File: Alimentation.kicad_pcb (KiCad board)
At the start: 2 copper layers, 50 x 50 mm, 21 parts, among them P1 Prise_Equilibrage, P2 Prise_Alim, P3 Prise_Batterie, P4 ConnecteurBippeur, P5 CONN_01X04, P6 CONN_01X02, P7 CONN_01X02, P8 CONN_01X02, U1 LD1084V

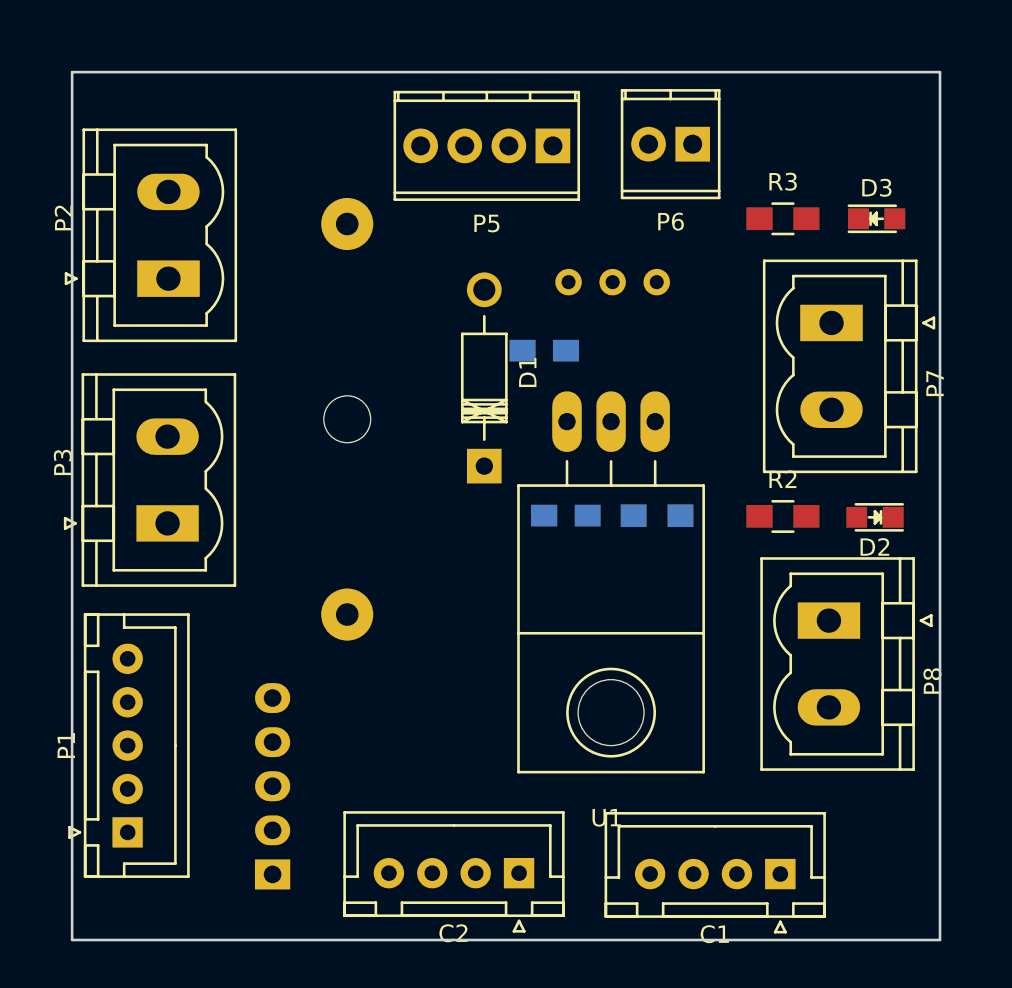
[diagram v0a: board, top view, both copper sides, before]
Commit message: prise en compte des changements dans la lib perso
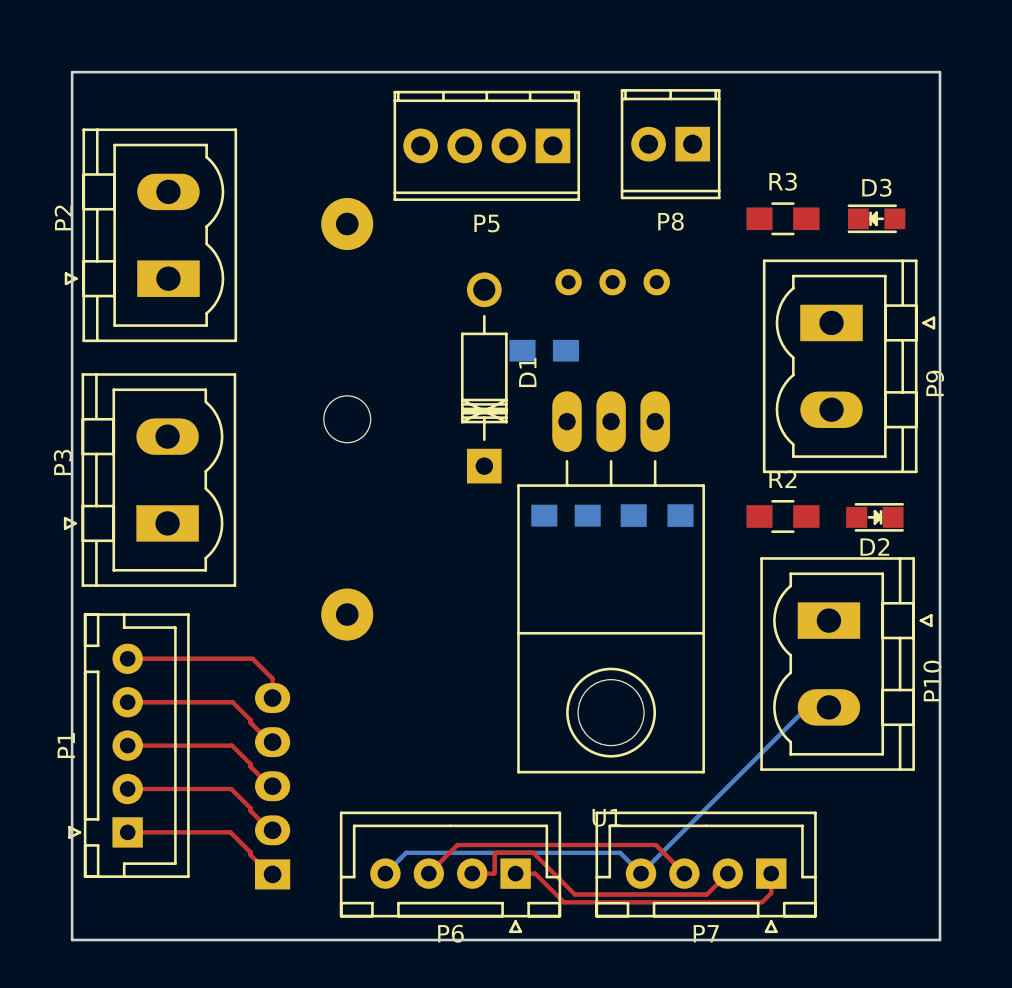
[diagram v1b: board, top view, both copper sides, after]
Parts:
- removed the C1 at (140.8, 96.2)
- removed the C2 at (125.8, 96.2)
- added P6: CAN_conn, Connectors_JST:JST_XH_B04B-XH-A_04x2.50mm_Straight, F.Cu at (125.5, 96.2)
- added P7: CAN_conn, Connectors_JST:JST_XH_B04B-XH-A_04x2.50mm_Straight, F.Cu at (140.3, 96.2)
- renumbered C3 to C1, C4 to C2, P8 to P10, P6 to P8, P7 to P9
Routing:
- net GND: track 0.00 -> 30.5 mm
- net CAN_H: track 0.00 -> 17.3 mm
- net +9V: track 0.00 -> 16.8 mm
- net CAN_L: track 0.00 -> 16.1 mm
- net Net-(P1-Pad5): track 0.00 -> 9.94 mm
- net Net-(P1-Pad1): track 0.00 -> 9.44 mm
- net Net-(P1-Pad2): track 0.00 -> 9.43 mm
- net Net-(P1-Pad3): track 0.00 -> 9.41 mm
- net Net-(P1-Pad4): track 0.00 -> 9.39 mm

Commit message: routage préliminaire (dirty)
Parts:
- moved C1 2.83 mm to (130.0, 66.0), turned to 0 degrees
- turned D3 to 180 degrees
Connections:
- P5 pad 1: Net-(F1-Pad2) -> GND
- P5 pad 2: GND -> Net-(F1-Pad2)
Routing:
- net GND: track 30.5 -> 160.3 mm
- net +9V: track 16.8 -> 66.7 mm
- net Net-(P3-Pad2): track 0.00 -> 27.2 mm
- net Net-(C1-Pad1): track 0.00 -> 23.7 mm
- net Net-(P2-Pad2): track 0.00 -> 16.4 mm
- net Non_régulé: track 0.00 -> 15.4 mm
- net Net-(R1-Pad2): track 0.00 -> 14.7 mm
- net Net-(D1-Pad1): track 0.00 -> 11.8 mm
- net Net-(F1-Pad2): track 0.00 -> 11.2 mm
- net Net-(D3-Pad2): track 0.00 -> 3.00 mm
- net Net-(D2-Pad2): track 0.00 -> 2.92 mm

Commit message: met la masse à l'extérieur
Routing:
- net GND: track 160.3 -> 171.0 mm
- net +9V: track 66.7 -> 69.5 mm
- net CAN_L: track 16.1 -> 16.9 mm
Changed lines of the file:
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@@
   (general
     (links 38)
-    (no_connects 15)
-    (area 99.924999 49.924999 150.075001 100.075001)
+    (no_connects 0)
+    (area 67.150001 22.3 150.825 102.395)
     (thickness 1.6)
     (drawings 6)
-    (tracks 133)
+    (tracks 130)
     (zones 0)
     (modules 21)
@@
     (arrow2b (pts (xy 75 50) (xy 75.586421 51.126504)))
   )
+  (segment (start 127.225 92.575) (end 125.55 94.25) (width 0.25) (layer F.Cu) (net 1))
+  (segment (start 125.55 94.25) (end 125.55 96.175) (width 0.25) (layer F.Cu) (net 1))
+  (segment (start 137.8 92.575) (end 127.225 92.575) (width 0.25) (layer F.Cu) (net 1))
+  (segment (start 140.275 96.175) (end 140.275 95.05) (width 0.25) (layer F.Cu) (net 1))
+  (segment (start 140.275 95.05) (end 137.8 92.575) (width 0.25) (layer F.Cu) (net 1))
   (segment (start 129.7 75.55) (end 130.7 75.55) (width 0.25) (layer B.Cu) (net 1))
   (segment (start 130.7 75.55) (end 131.05 75.2) (width 0.25) (layer B.Cu) (net 1))
@@
   (segment (start 139.6 75.6) (end 139.6 78.35) (width 0.25) (layer F.Cu) (net 1))
   (segment (start 139.6 78.35) (end 142.85 81.6) (width 0.25) (layer F.Cu) (net 1))
-  (segment (start 126.675 96.175) (end 125.55 96.175) (width 0.25) (layer F.Cu) (net 1))
-  (segment (start 139.749988 97.825012) (end 128.325012 97.825012) (width 0.25) (layer F.Cu) (net 1))
-  (segment (start 140.275 97.3) (end 139.749988 97.825012) (width 0.25) (layer F.Cu) (net 1))
-  (segment (start 140.275 96.175) (end 140.275 97.3) (width 0.25) (layer F.Cu) (net 1))
-  (segment (start 128.325012 97.825012) (end 126.675 96.175) (width 0.25) (layer F.Cu) (net 1))
-  (segment (start 135.275 96.175) (end 133.624988 94.524988) (width 0.25) (layer F.Cu) (net 2))
-  (segment (start 133.624988 94.524988) (end 122.200012 94.524988) (width 0.25) (layer F.Cu) (net 2))
-  (segment (start 122.200012 94.524988) (end 121.424999 95.300001) (width 0.25) (layer F.Cu) (net 2))
-  (segment (start 121.424999 95.300001) (end 120.55 96.175) (width 0.25) (layer F.Cu) (net 2))
-  (segment (start 124.349999 96.112437) (end 124.287436 96.175) (width 0.25) (layer F.Cu) (net 3))
-  (segment (start 124.349999 95.039999) (end 124.349999 96.112437) (width 0.25) (layer F.Cu) (net 3))
-  (segment (start 126.563595 94.974999) (end 124.414999 94.974999) (width 0.25) (layer F.Cu) (net 3))
-  (segment (start 128.963597 97.375001) (end 126.563595 94.974999) (width 0.25) (layer F.Cu) (net 3))
-  (segment (start 136.574999 97.375001) (end 128.963597 97.375001) (width 0.25) (layer F.Cu) (net 3))
-  (segment (start 137.775 96.175) (end 136.574999 97.375001) (width 0.25) (layer F.Cu) (net 3))
-  (segment (start 124.287436 96.175) (end 123.05 96.175) (width 0.25) (layer F.Cu) (net 3))
-  (segment (start 124.414999 94.974999) (end 124.349999 95.039999) (width 0.25) (layer F.Cu) (net 3))
+  (segment (start 121.112564 97.975) (end 133.475 97.975) (width 0.25) (layer B.Cu) (net 2))
+  (segment (start 133.475 97.975) (end 135.275 96.175) (width 0.25) (layer B.Cu) (net 2))
+  (segment (start 120.55 96.175) (end 120.55 97.412436) (width 0.25) (layer B.Cu) (net 2))
+  (segment (start 120.55 97.412436) (end 121.112564 97.975) (width 0.25) (layer B.Cu) (net 2))
+  (segment (start 123.05 96.175) (end 125.65 93.575) (width 0.25) (layer B.Cu) (net 3))
+  (segment (start 125.65 93.575) (end 135.175 93.575) (width 0.25) (layer B.Cu) (net 3))
+  (segment (start 135.175 93.575) (end 137.775 96.175) (width 0.25) (layer B.Cu) (net 3))
+  (segment (start 130.4 98.55) (end 120.425 98.55) (width 0.25) (layer F.Cu) (net 4))
+  (segment (start 120.425 98.55) (end 118.05 96.175) (width 0.25) (layer F.Cu) (net 4))
+  (segment (start 132.775 96.175) (end 130.4 98.55) (width 0.25) (layer F.Cu) (net 4))
+  (segment (start 142.65 98.55) (end 135.15 98.55) (width 0.25) (layer F.Cu) (net 4))
+  (segment (start 135.15 98.55) (end 132.775 96.175) (width 0.25) (layer F.Cu) (net 4))
+  (segment (start 143.6 97.6) (end 142.65 98.55) (width 0.25) (layer F.Cu) (net 4))
+  (segment (start 143.6 86.6) (end 143.6 97.6) (width 0.25) (layer F.Cu) (net 4))
   (segment (start 139.9 64.25) (end 139.9 67.3) (width 0.25) (layer B.Cu) (net 4))
   (segment (start 137.575 76.125) (end 137.575 74.875) (width 0.25) (layer B.Cu) (net 4))
@@
   (segment (start 147.29804 75.65) (end 147.29804 72.24804) (width 0.25) (layer F.Cu) (net 4))
   (segment (start 147.29804 72.24804) (end 144.5 69.45) (width 0.25) (layer F.Cu) (net 4))
-  (segment (start 132.775 96.175) (end 142.35 86.6) (width 0.25) (layer B.Cu) (net 4))
   (segment (start 142.35 86.6) (end 143.6 86.6) (width 0.25) (layer B.Cu) (net 4))
-  (segment (start 132.775 96.175) (end 131.574999 94.974999) (width 0.25) (layer B.Cu) (net 4))
-  (segment (start 119.250001 94.974999) (end 118.924999 95.300001) (width 0.25) (layer B.Cu) (net 4))
-  (segment (start 131.574999 94.974999) (end 119.250001 94.974999) (width 0.25) (layer B.Cu) (net 4))
-  (segment (start 118.924999 95.300001) (end 118.05 96.175) (width 0.25) (layer B.Cu) (net 4))
   (segment (start 115.85 81.25) (end 123.74746 73.35254) (width 0.25) (layer F.Cu) (net 5))
   (segment (start 123.74746 73.35254) (end 123.74746 72.7) (width 0.25) (layer F.Cu) (net 5))

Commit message: routage terminé ?
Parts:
- F1, R1, RV1: moved to F.Cu
- P10, P2, P3, P9: footprint Connectors_Phoenix:PhoenixContact_MSTBVA-G_02x5.00mm_Vertical -> Connectors_Phoenix:PhoenixContact_MC-G_02x3.50mm_Angled
- P5: footprint Terminal_Blocks:TerminalBlock_Pheonix_MPT-2.54mm_4pol -> Connectors_Phoenix:PhoenixContact_MC-G_04x3.50mm_Angled
- P8: footprint Terminal_Blocks:TerminalBlock_Pheonix_MPT-2.54mm_2pol -> Connectors_Phoenix:PhoenixContact_MC-G_02x3.50mm_Angled
- moved D1 15.3 mm to (123.0, 88.0)
- moved R3 11.1 mm to (140.0, 69.5), turned to 90 degrees
- moved P8 10.4 mm to (146.0, 56.0)
- moved C2 9.18 mm to (130.0, 66.5)
- moved P9 7.55 mm to (144.0, 72.0), turned to 90 degrees
- moved P5 7.51 mm to (135.0, 56.0)
- moved R1 6.03 mm to (137.0, 70.5), turned to 90 degrees
- moved P3 6.02 mm to (106.0, 70.0), turned to 270 degrees
- moved D3 5.87 mm to (144.5, 64.0)
- moved C1 5.44 mm to (125.5, 69.0), turned to 90 degrees
- moved P10 4.92 mm to (144.0, 86.5), turned to 90 degrees
- moved P2 3.93 mm to (106.0, 58.0), turned to 270 degrees
- moved D2 3.47 mm to (144.5, 78.7)
- moved P1 3.05 mm to (105.2, 91.5)
- moved R2 2.02 mm to (139.5, 77.0)
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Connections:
- P10 pad 1: +9V -> GND
- P10 pad 2: GND -> +9V
- P9 pad 1: Non_régulé -> GND
- P9 pad 2: GND -> Non_régulé
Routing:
- net Net-(C1-Pad1): track 23.7 -> 41.1 mm
- net Net-(F1-Pad2): track 11.2 -> 19.4 mm
- net Net-(P2-Pad2): track 16.4 -> 21.3 mm
- net CAN_H: track 16.9 -> 21.7 mm
- net CAN_L: track 16.9 -> 21.6 mm
- net Net-(P3-Pad2): track 27.2 -> 31.3 mm
- net GND: track 171.0 -> 174.4 mm
- net Non_régulé: track 15.4 -> 18.3 mm
- net Net-(D3-Pad2): track 3.00 -> 5.76 mm
- net +9V: track 69.5 -> 71.7 mm
- net Net-(R1-Pad2): track 14.7 -> 12.6 mm
- net Net-(P1-Pad5): track 9.94 -> 8.03 mm
- net Net-(P1-Pad2): track 9.43 -> 8.08 mm
- net Net-(P1-Pad4): track 9.39 -> 8.04 mm
- net Net-(P1-Pad3): track 9.41 -> 8.06 mm
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- added copper zone on B.Cu, net GND
- added copper zone on F.Cu, net GND
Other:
- net class DRC added: clearance 0.65, trace_width 0.5, via_dia 0.6, via_drill 0.4
- net class Interm added: clearance 0.4, trace_width 0.5, via_dia 0.6, via_drill 0.4
- net class PWR added: clearance 0.8, trace_width 1.5, via_dia 0.6, via_drill 0.4

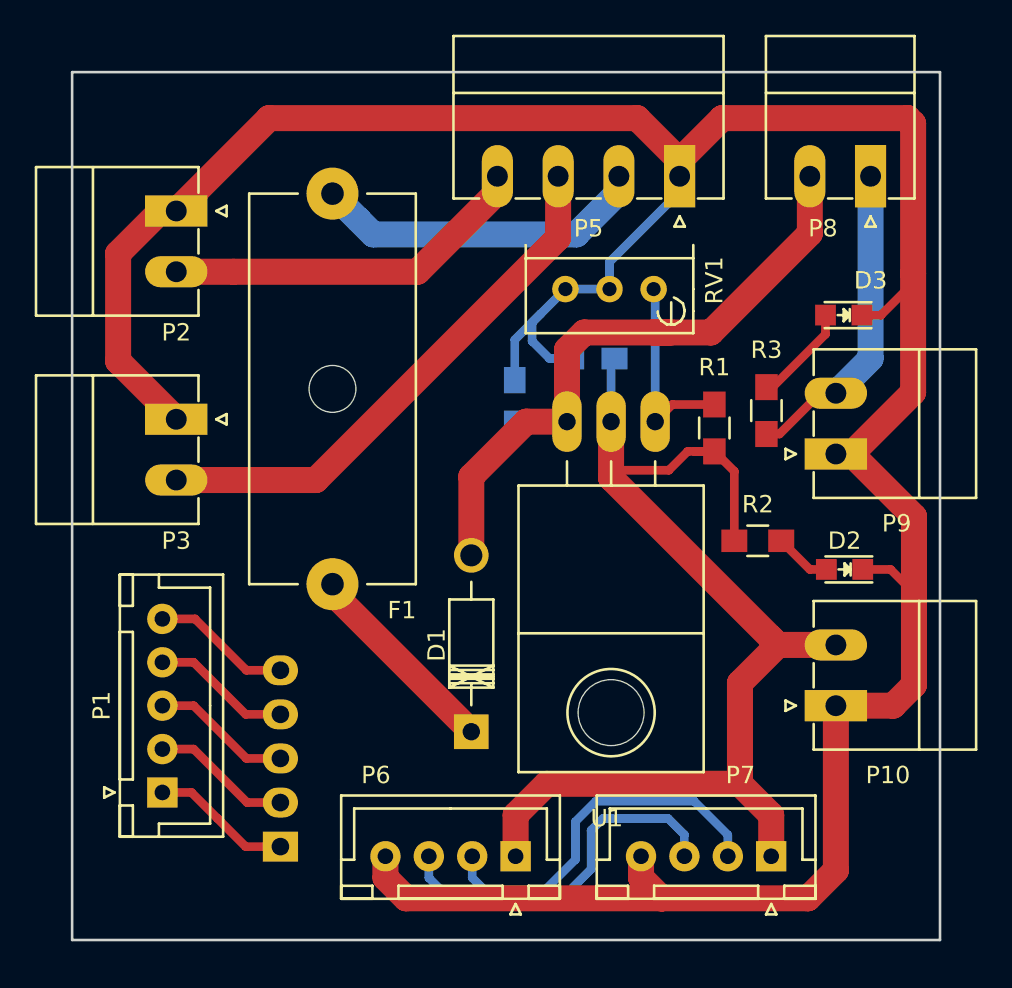
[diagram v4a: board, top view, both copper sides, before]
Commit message: ajoute les trous pour les vis
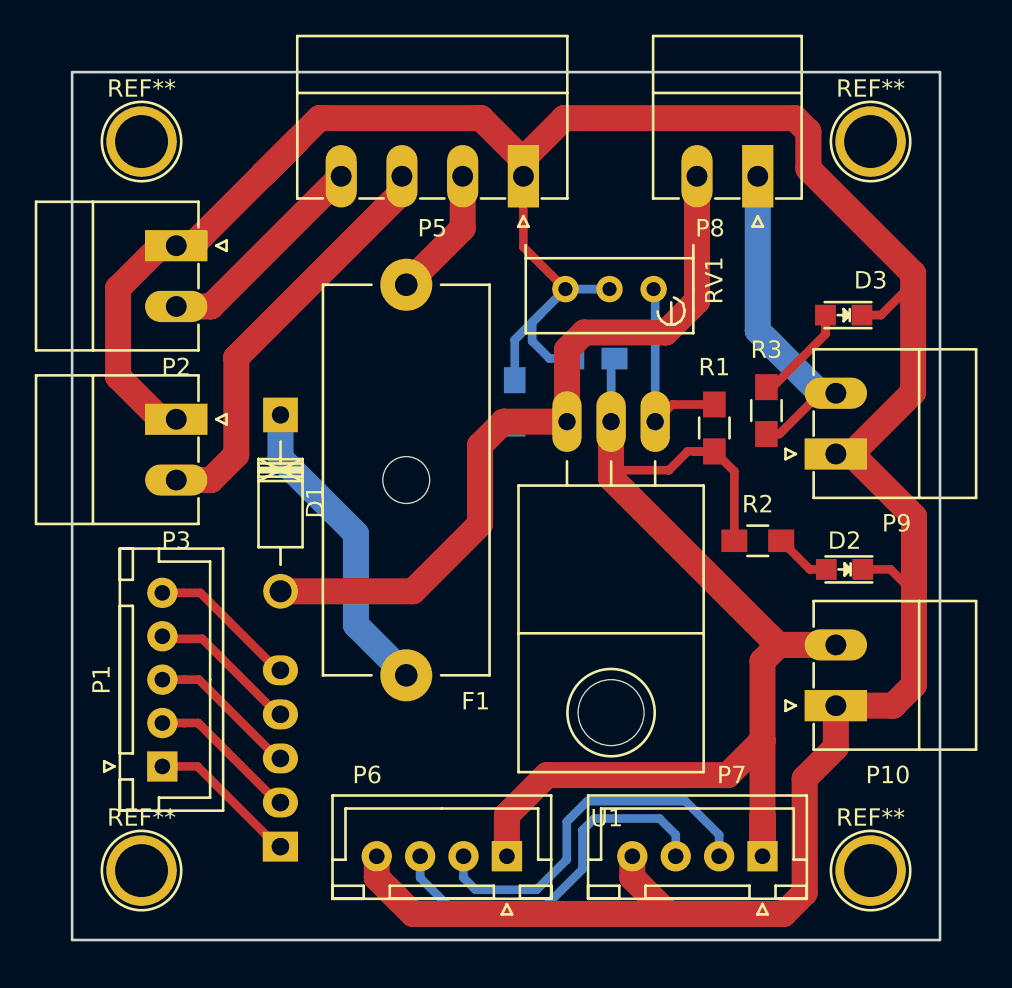
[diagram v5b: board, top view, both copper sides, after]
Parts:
- added REF**: 1pin, Connect:1pin, F.Cu at (104.0, 96.0)
- added REF**: 1pin, Connect:1pin, F.Cu at (104.0, 54.0)
- added REF**: 1pin, Connect:1pin, F.Cu at (146.0, 96.0)
- added REF**: 1pin, Connect:1pin, F.Cu at (146.0, 54.0)
- moved D1 21.3 mm to (112.0, 69.8), turned to 270 degrees
- moved P5 9.00 mm to (126.0, 56.0)
- moved F1 6.75 mm to (119.2, 84.8)
- moved P8 6.50 mm to (139.5, 56.0)
- moved P2 2.00 mm to (106.0, 60.0)
- moved P1 1.50 mm to (105.2, 90.0)
- moved P6 0.50 mm to (125.0, 95.2)
- moved P7 0.50 mm to (139.8, 95.2)
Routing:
- net Net-(F1-Pad2): track 19.4 -> 7.60 mm
- net Net-(P2-Pad2): track 21.3 -> 12.6 mm
- net Net-(P3-Pad2): track 31.3 -> 24.1 mm
- net +9V: track 71.7 -> 78.9 mm
- net Net-(D1-Pad1): track 11.8 -> 18.0 mm
- net Net-(C1-Pad1): track 41.1 -> 46.8 mm
- net Non_régulé: track 18.3 -> 20.7 mm
- net GND: track 174.4 -> 176.8 mm
- net Net-(P1-Pad5): track 8.03 -> 8.65 mm
- net Net-(P1-Pad3): track 8.06 -> 8.68 mm
- net Net-(P1-Pad2): track 8.08 -> 8.70 mm
- net Net-(P1-Pad1): track 8.09 -> 8.71 mm
- net Net-(P1-Pad4): track 8.04 -> 8.60 mm
